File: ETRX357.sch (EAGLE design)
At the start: 8 parts

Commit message: porzadki w plikach
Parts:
- renumbered U$1 to ETRX357
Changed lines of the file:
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@@
 <?xml version="1.0" encoding="utf-8"?>
 <!DOCTYPE eagle SYSTEM "eagle.dtd">
-<eagle version="6.3">
+<eagle version="6.2">
 <drawing>
 <settings>
@@
 </classes>
 <parts>
-<part name="U$1" library="etrx357_logical" deviceset="ETRX357*" device="" technology="HR"/>
+<part name="ETRX357" library="etrx357_logical" deviceset="ETRX357*" device="" technology="HR"/>
 <part name="GND1" library="SparkFun-Aesthetics" deviceset="GND" device=""/>
 <part name="SUPPLY1" library="SparkFun-Aesthetics" deviceset="3.3V" device=""/>
@@
 </plain>
 <instances>
-<instance part="U$1" gate="G$1" x="33.02" y="66.04"/>
+<instance part="ETRX357" gate="G$1" x="33.02" y="66.04"/>
 <instance part="GND1" gate="1" x="53.34" y="40.64"/>
 <instance part="SUPPLY1" gate="G$1" x="66.04" y="78.74"/>
@@
 <net name="TXD" class="0">
 <segment>
-<pinref part="U$1" gate="G$1" pin="PB1"/>
+<pinref part="ETRX357" gate="G$1" pin="PB1"/>
 <wire x1="10.16" y1="55.88" x2="5.08" y2="55.88" width="0.1524" layer="91"/>
 <label x="0" y="55.88" size="1.778" layer="95"/>
@@
 <net name="RXD" class="0">
 <segment>
-<pinref part="U$1" gate="G$1" pin="PB2"/>
+<pinref part="ETRX357" gate="G$1" pin="PB2"/>
 <wire x1="10.16" y1="53.34" x2="5.08" y2="53.34" width="0.1524" layer="91"/>
 <label x="0" y="53.34" size="1.778" layer="95"/>
@@
 <net name="GND" class="0">
 <segment>
-<pinref part="U$1" gate="G$1" pin="GND@6"/>
+<pinref part="ETRX357" gate="G$1" pin="GND@6"/>
 <wire x1="53.34" y1="60.96" x2="53.34" y2="58.42" width="0.1524" layer="91"/>
 <junction x="53.34" y="60.96"/>
-<pinref part="U$1" gate="G$1" pin="GND@5"/>
+<pinref part="ETRX357" gate="G$1" pin="GND@5"/>
 <junction x="53.34" y="58.42"/>
 <wire x1="53.34" y1="58.42" x2="53.34" y2="55.88" width="0.1524" layer="91"/>
-<pinref part="U$1" gate="G$1" pin="GND@4"/>
+<pinref part="ETRX357" gate="G$1" pin="GND@4"/>
 <junction x="53.34" y="55.88"/>
 <wire x1="53.34" y1="55.88" x2="53.34" y2="53.34" width="0.1524" layer="91"/>
-<pinref part="U$1" gate="G$1" pin="GND@3"/>
+<pinref part="ETRX357" gate="G$1" pin="GND@3"/>
 <junction x="53.34" y="53.34"/>
 <wire x1="53.34" y1="53.34" x2="53.34" y2="50.8" width="0.1524" layer="91"/>
-<pinref part="U$1" gate="G$1" pin="GND@2"/>
+<pinref part="ETRX357" gate="G$1" pin="GND@2"/>
 <junction x="53.34" y="50.8"/>
 <wire x1="53.34" y1="50.8" x2="53.34" y2="48.26" width="0.1524" layer="91"/>
-<pinref part="U$1" gate="G$1" pin="GND@1"/>
+<pinref part="ETRX357" gate="G$1" pin="GND@1"/>
 <junction x="53.34" y="48.26"/>
 <wire x1="53.34" y1="48.26" x2="53.34" y2="43.18" width="0.1524" layer="91"/>
@@
 <net name="3.3V" class="0">
 <segment>
-<pinref part="U$1" gate="G$1" pin="VCC"/>
+<pinref part="ETRX357" gate="G$1" pin="VCC"/>
 <wire x1="53.34" y1="78.74" x2="66.04" y2="78.74" width="0.1524" layer="91"/>
 <pinref part="SUPPLY1" gate="G$1" pin="3.3V"/>
@@
 <net name="N$1" class="0">
 <segment>
-<pinref part="U$1" gate="G$1" pin="PC6"/>
+<pinref part="ETRX357" gate="G$1" pin="PC6"/>
 <wire x1="10.16" y1="22.86" x2="5.08" y2="22.86" width="0.1524" layer="91"/>
 <wire x1="5.08" y1="22.86" x2="5.08" y2="27.94" width="0.1524" layer="91"/>
@@
 <net name="N$2" class="0">
 <segment>
-<pinref part="U$1" gate="G$1" pin="PC7"/>
+<pinref part="ETRX357" gate="G$1" pin="PC7"/>
 <wire x1="10.16" y1="20.32" x2="2.54" y2="20.32" width="0.1524" layer="91"/>
 <pinref part="LED2" gate="G$1" pin="A"/>
@@
 <net name="N$3" class="0">
 <segment>
-<pinref part="U$1" gate="G$1" pin="PB7"/>
+<pinref part="ETRX357" gate="G$1" pin="PB7"/>
 <pinref part="LED3" gate="G$1" pin="A"/>
 </segment>

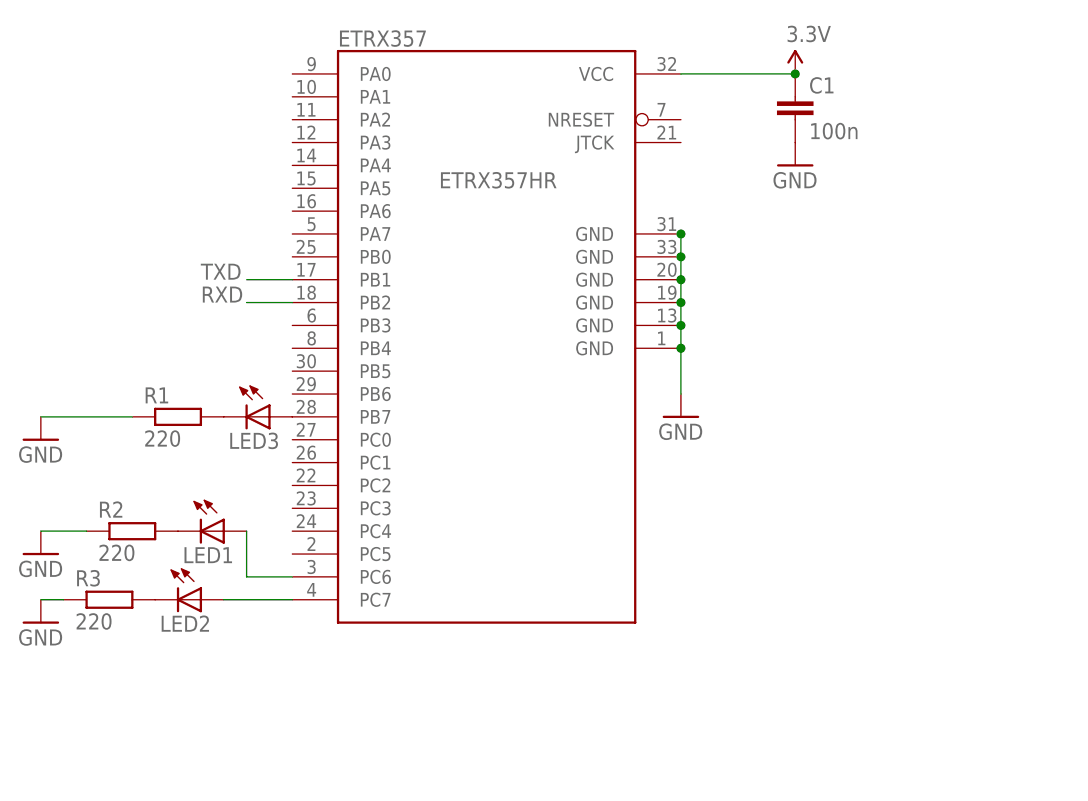
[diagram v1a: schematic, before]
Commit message: dodane obwodki z nazwami dla poszczegolnych elementow
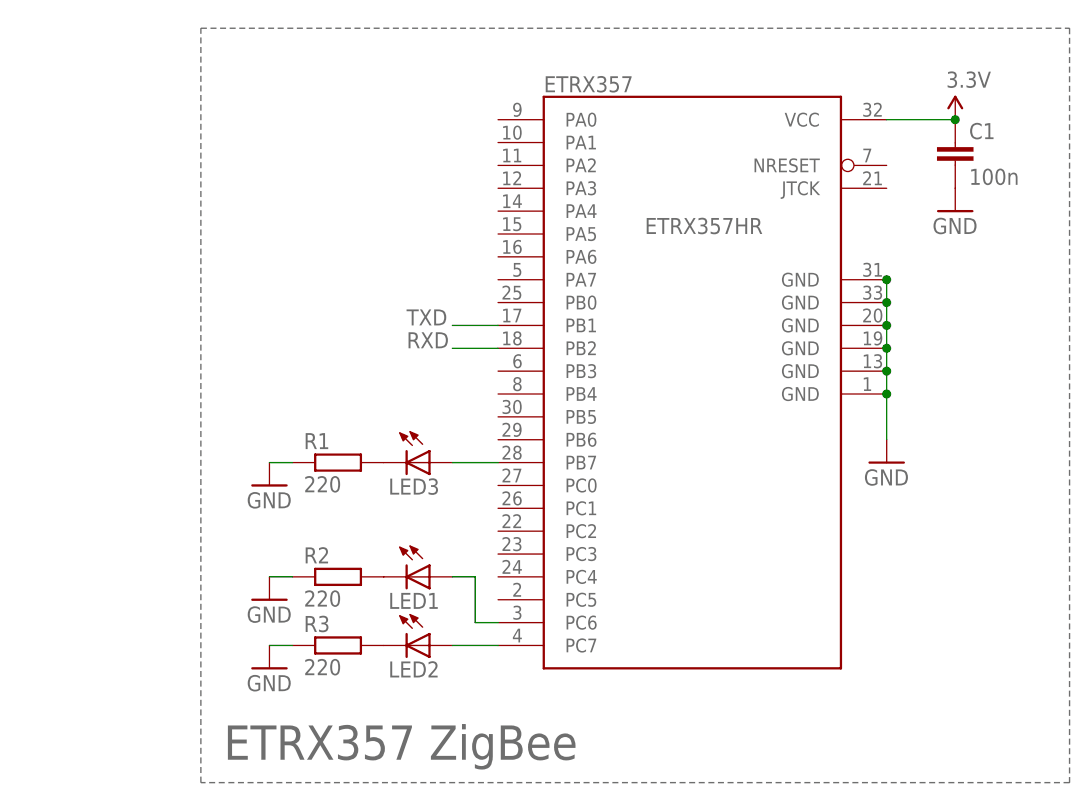
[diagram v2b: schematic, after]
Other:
- note added: "ETRX357 ZigBee"
- moved on the sheet: C1, ETRX357, LED1, LED2, LED3, R1, R2, R3
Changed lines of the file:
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@@
 <sheet>
 <plain>
+<wire x1="0" y1="83.82" x2="96.52" y2="83.82" width="0.1524" layer="95" style="shortdash"/>
+<wire x1="96.52" y1="83.82" x2="96.52" y2="0" width="0.1524" layer="95" style="shortdash"/>
+<wire x1="96.52" y1="0" x2="0" y2="0" width="0.1524" layer="95" style="shortdash"/>
+<wire x1="0" y1="0" x2="0" y2="83.82" width="0.1524" layer="95" style="shortdash"/>
+<text x="2.54" y="2.54" size="3.81" layer="95">ETRX357 ZigBee</text>
 </plain>
 <instances>
-<instance part="ETRX357" gate="G$1" x="33.02" y="66.04"/>
-<instance part="GND1" gate="1" x="53.34" y="40.64"/>
-<instance part="SUPPLY1" gate="G$1" x="66.04" y="78.74"/>
-<instance part="C1" gate="G$1" x="66.04" y="76.2"/>
-<instance part="GND2" gate="1" x="66.04" y="68.58"/>
-<instance part="LED1" gate="G$1" x="2.54" y="27.94" rot="R270"/>
-<instance part="LED2" gate="G$1" x="0" y="20.32" rot="R270"/>
-<instance part="LED3" gate="G$1" x="7.62" y="40.64" rot="R270"/>
-<instance part="R1" gate="G$1" x="-2.54" y="40.64"/>
-<instance part="R2" gate="G$1" x="-7.62" y="27.94"/>
-<instance part="R3" gate="G$1" x="-10.16" y="20.32"/>
-<instance part="GND3" gate="1" x="-17.78" y="38.1"/>
-<instance part="GND4" gate="1" x="-17.78" y="25.4"/>
-<instance part="GND5" gate="1" x="-17.78" y="17.78"/>
+<instance part="ETRX357" gate="G$1" x="55.88" y="60.96"/>
+<instance part="GND1" gate="1" x="76.2" y="35.56"/>
+<instance part="SUPPLY1" gate="G$1" x="83.82" y="73.66"/>
+<instance part="C1" gate="G$1" x="83.82" y="71.12"/>
+<instance part="GND2" gate="1" x="83.82" y="63.5"/>
+<instance part="LED1" gate="G$1" x="25.4" y="22.86" rot="R270"/>
+<instance part="LED2" gate="G$1" x="25.4" y="15.24" rot="R270"/>
+<instance part="LED3" gate="G$1" x="25.4" y="35.56" rot="R270"/>
+<instance part="R1" gate="G$1" x="15.24" y="35.56"/>
+<instance part="R2" gate="G$1" x="15.24" y="22.86"/>
+<instance part="R3" gate="G$1" x="15.24" y="15.24"/>
+<instance part="GND3" gate="1" x="7.62" y="33.02"/>
+<instance part="GND4" gate="1" x="7.62" y="20.32"/>
+<instance part="GND5" gate="1" x="7.62" y="12.7"/>
 </instances>
 <busses>
@@
 <segment>
 <pinref part="ETRX357" gate="G$1" pin="PB1"/>
-<wire x1="10.16" y1="55.88" x2="5.08" y2="55.88" width="0.1524" layer="91"/>
-<label x="0" y="55.88" size="1.778" layer="95"/>
+<wire x1="33.02" y1="50.8" x2="27.94" y2="50.8" width="0.1524" layer="91"/>
+<label x="22.86" y="50.8" size="1.778" layer="95"/>
 </segment>
 </net>
@@
 <segment>
 <pinref part="ETRX357" gate="G$1" pin="PB2"/>
-<wire x1="10.16" y1="53.34" x2="5.08" y2="53.34" width="0.1524" layer="91"/>
-<label x="0" y="53.34" size="1.778" layer="95"/>
+<wire x1="33.02" y1="48.26" x2="27.94" y2="48.26" width="0.1524" layer="91"/>
+<label x="22.86" y="48.26" size="1.778" layer="95"/>
 </segment>
 </net>
@@
 <segment>
 <pinref part="ETRX357" gate="G$1" pin="GND@6"/>
-<wire x1="53.34" y1="60.96" x2="53.34" y2="58.42" width="0.1524" layer="91"/>
-<junction x="53.34" y="60.96"/>
+<wire x1="76.2" y1="55.88" x2="76.2" y2="53.34" width="0.1524" layer="91"/>
+<junction x="76.2" y="55.88"/>
 <pinref part="ETRX357" gate="G$1" pin="GND@5"/>
-<junction x="53.34" y="58.42"/>
-<wire x1="53.34" y1="58.42" x2="53.34" y2="55.88" width="0.1524" layer="91"/>
+<junction x="76.2" y="53.34"/>
+<wire x1="76.2" y1="53.34" x2="76.2" y2="50.8" width="0.1524" layer="91"/>
 <pinref part="ETRX357" gate="G$1" pin="GND@4"/>
-<junction x="53.34" y="55.88"/>
-<wire x1="53.34" y1="55.88" x2="53.34" y2="53.34" width="0.1524" layer="91"/>
+<junction x="76.2" y="50.8"/>
+<wire x1="76.2" y1="50.8" x2="76.2" y2="48.26" width="0.1524" layer="91"/>
 <pinref part="ETRX357" gate="G$1" pin="GND@3"/>
-<junction x="53.34" y="53.34"/>
-<wire x1="53.34" y1="53.34" x2="53.34" y2="50.8" width="0.1524" layer="91"/>
+<junction x="76.2" y="48.26"/>
+<wire x1="76.2" y1="48.26" x2="76.2" y2="45.72" width="0.1524" layer="91"/>
 <pinref part="ETRX357" gate="G$1" pin="GND@2"/>
-<junction x="53.34" y="50.8"/>
-<wire x1="53.34" y1="50.8" x2="53.34" y2="48.26" width="0.1524" layer="91"/>
+<junction x="76.2" y="45.72"/>
+<wire x1="76.2" y1="45.72" x2="76.2" y2="43.18" width="0.1524" layer="91"/>
 <pinref part="ETRX357" gate="G$1" pin="GND@1"/>
-<junction x="53.34" y="48.26"/>
-<wire x1="53.34" y1="48.26" x2="53.34" y2="43.18" width="0.1524" layer="91"/>
+<junction x="76.2" y="43.18"/>
+<wire x1="76.2" y1="43.18" x2="76.2" y2="38.1" width="0.1524" layer="91"/>
 <pinref part="GND1" gate="1" pin="GND"/>
 </segment>
@@
 <segment>
 <pinref part="R1" gate="G$1" pin="1"/>
-<wire x1="-7.62" y1="40.64" x2="-17.78" y2="40.64" width="0.1524" layer="91"/>
+<wire x1="10.16" y1="35.56" x2="7.62" y2="35.56" width="0.1524" layer="91"/>
 <pinref part="GND3" gate="1" pin="GND"/>
 </segment>
 <segment>
 <pinref part="R2" gate="G$1" pin="1"/>
-<wire x1="-12.7" y1="27.94" x2="-17.78" y2="27.94" width="0.1524" layer="91"/>
+<wire x1="10.16" y1="22.86" x2="7.62" y2="22.86" width="0.1524" layer="91"/>
 <pinref part="GND4" gate="1" pin="GND"/>
 </segment>
@@
 <pinref part="R3" gate="G$1" pin="1"/>
 <pinref part="GND5" gate="1" pin="GND"/>
-<wire x1="-17.78" y1="20.32" x2="-15.24" y2="20.32" width="0.1524" layer="91"/>
+<wire x1="7.62" y1="15.24" x2="10.16" y2="15.24" width="0.1524" layer="91"/>
 </segment>
 </net>
@@
 <segment>
 <pinref part="ETRX357" gate="G$1" pin="VCC"/>
-<wire x1="53.34" y1="78.74" x2="66.04" y2="78.74" width="0.1524" layer="91"/>
+<wire x1="76.2" y1="73.66" x2="83.82" y2="73.66" width="0.1524" layer="91"/>
 <pinref part="SUPPLY1" gate="G$1" pin="3.3V"/>
 <pinref part="C1" gate="G$1" pin="1"/>
-<junction x="66.04" y="78.74"/>
+<junction x="83.82" y="73.66"/>
 </segment>
 </net>
@@
 <segment>
 <pinref part="ETRX357" gate="G$1" pin="PC6"/>
-<wire x1="10.16" y1="22.86" x2="5.08" y2="22.86" width="0.1524" layer="91"/>
-<wire x1="5.08" y1="22.86" x2="5.08" y2="27.94" width="0.1524" layer="91"/>
+<wire x1="33.02" y1="17.78" x2="30.48" y2="17.78" width="0.1524" layer="91"/>
+<wire x1="30.48" y1="17.78" x2="30.48" y2="22.86" width="0.1524" layer="91"/>
+<wire x1="30.48" y1="22.86" x2="27.94" y2="22.86" width="0.1524" layer="91"/>
 <pinref part="LED1" gate="G$1" pin="A"/>
 </segment>
@@
 <segment>
 <pinref part="ETRX357" gate="G$1" pin="PC7"/>
-<wire x1="10.16" y1="20.32" x2="2.54" y2="20.32" width="0.1524" layer="91"/>
+<wire x1="33.02" y1="15.24" x2="27.94" y2="15.24" width="0.1524" layer="91"/>
 <pinref part="LED2" gate="G$1" pin="A"/>
 </segment>
@@
 <pinref part="ETRX357" gate="G$1" pin="PB7"/>
 <pinref part="LED3" gate="G$1" pin="A"/>
+<wire x1="27.94" y1="35.56" x2="33.02" y2="35.56" width="0.1524" layer="91"/>
 </segment>
 </net>
